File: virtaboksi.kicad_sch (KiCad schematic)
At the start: 21 parts, among them J1 Conn_01x03_Female, J2 Conn_01x02_Female, J3 Conn_01x02_Female, J4 Conn_01x02_Female, J5 Conn_01x02_Female, J6 Conn_01x02_Female, J7 Conn_01x02_Female, Q1 IRF9540N, Q2 IRF9540N, Q3 IRF9540N

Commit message: Fine-tuning of the board
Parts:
- J1: renamed from J2; footprint Connector_Phoenix_MSTB:PhoenixContact_MSTBA_2,5_2-G_1x02_P5.00mm_Horizontal -> Connector_Phoenix_MC:PhoenixContact_MCV_1,5_2-G-3.81_1x02_P3.81mm_Vertical
- J2: renamed from J1; footprint Connector_Phoenix_MSTB:PhoenixContact_MSTBA_2,5_3-G_1x03_P5.00mm_Horizontal -> Connector_Phoenix_MC:PhoenixContact_MCV_1,5_3-G-3.81_1x03_P3.81mm_Vertical
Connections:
- net BAT GOOD: now also J1.2 (Pin_2), J2.1 (Pin_1); no longer J1.1 (Pin_1), J2.3 (Pin_3)
- net HOME: now also J2.3 (Pin_3); no longer J2.1 (Pin_1)
- net at F1.2: now also J1.1 (Pin_1); no longer J1.2 (Pin_2)
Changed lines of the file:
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@@
-    (stroke (width 0) (type default) (color 0 0 0 0))
-  )
-  (wire (pts (xy 165.1 113.03) (xy 163.83 113.03))
     (stroke (width 0) (type default) (color 0 0 0 0))
   )
@@
     (stroke (width 0) (type default) (color 0 0 0 0))
   )
-  (wire (pts (xy 152.4 93.98) (xy 165.1 93.98))
+  (wire (pts (xy 152.4 99.06) (xy 165.1 99.06))
     (stroke (width 0) (type default) (color 0 0 0 0))
   )
@@
     (stroke (width 0) (type default) (color 0 0 0 0))
   )
-  (wire (pts (xy 149.86 99.06) (xy 165.1 99.06))
-    (stroke (width 0) (type default) (color 0 0 0 0))
-  )
   (wire (pts (xy 64.77 72.39) (xy 76.2 72.39))
     (stroke (width 0) (type default) (color 0 0 0 0))
@@
     (stroke (width 0) (type default) (color 0 0 0 0))
   )
+  (wire (pts (xy 165.1 110.49) (xy 163.83 110.49))
+    (stroke (width 0) (type default) (color 0 0 0 0))
+  )
   (wire (pts (xy 62.23 49.53) (xy 64.77 49.53))
     (stroke (width 0) (type default) (color 0 0 0 0))
   )
-  (wire (pts (xy 163.83 113.03) (xy 163.83 115.57))
+  (wire (pts (xy 163.83 110.49) (xy 163.83 115.57))
     (stroke (width 0) (type default) (color 0 0 0 0))
   )
@@
     (stroke (width 0) (type default) (color 0 0 0 0))
   )
+  (wire (pts (xy 165.1 93.98) (xy 149.86 93.98))
+    (stroke (width 0) (type default) (color 0 0 0 0))
+  )
   (wire (pts (xy 76.2 72.39) (xy 76.2 78.74))
     (stroke (width 0) (type default) (color 0 0 0 0))
@@
     (stroke (width 0) (type default) (color 0 0 0 0))
   )
+  (wire (pts (xy 165.1 113.03) (xy 149.86 113.03))
+    (stroke (width 0) (type default) (color 0 0 0 0))
+  )
   (wire (pts (xy 44.45 49.53) (xy 54.61 49.53))
     (stroke (width 0) (type default) (color 0 0 0 0))
   )
-  (wire (pts (xy 149.86 110.49) (xy 149.86 99.06))
+  (wire (pts (xy 149.86 93.98) (xy 149.86 113.03))
     (stroke (width 0) (type default) (color 0 0 0 0))
   )
@@
   )
   (wire (pts (xy 62.23 83.82) (xy 64.77 83.82))
-    (stroke (width 0) (type default) (color 0 0 0 0))
-  )
-  (wire (pts (xy 149.86 110.49) (xy 165.1 110.49))
     (stroke (width 0) (type default) (color 0 0 0 0))
   )
@@
     (effects (font (size 1.27 1.27)) (justify left bottom))
   )
-  (label "BAT GOOD" (at 152.4 110.49 0)
+  (label "BAT GOOD" (at 152.4 113.03 0)
     (effects (font (size 1.27 1.27)) (justify left bottom))
   )
@@
     (effects (font (size 1.27 1.27)) (justify left bottom))
   )
-  (label "HOME" (at 152.4 93.98 0)
+  (label "HOME" (at 152.4 99.06 0)
     (effects (font (size 1.27 1.27)) (justify left bottom))
   )
@@
   (symbol (lib_id "Connector:Conn_01x03_Female") (at 170.18 96.52 0) (unit 1)
     (in_bom yes) (on_board yes) (fields_autoplaced)
-    (property "Reference" "J1" (id 0) (at 170.8912 95.6853 0)
+    (property "Reference" "J2" (id 0) (at 170.8912 95.6853 0)
       (effects (font (size 1.27 1.27)) (justify left))
     )
@@
       (effects (font (size 1.27 1.27)) (justify left))
     )
-    (property "Footprint" "Connector_Phoenix_MSTB:PhoenixContact_MSTBA_2,5_3-G_1x03_P5.00mm_Horizontal" (id 2) (at 170.18 96.52 0)
+    (property "Footprint" "Connector_Phoenix_MC:PhoenixContact_MCV_1,5_3-G-3.81_1x03_P3.81mm_Vertical" (id 2) (at 170.18 96.52 0)
       (effects (font (size 1.27 1.27)) hide)
     )
@@
   (symbol (lib_id "Connector:Conn_01x02_Female") (at 170.18 110.49 0) (unit 1)
     (in_bom yes) (on_board yes)
-    (property "Reference" "J2" (id 0) (at 170.8912 110.9253 0)
+    (property "Reference" "J1" (id 0) (at 170.8912 110.9253 0)
       (effects (font (size 1.27 1.27)) (justify left))
     )
@@
       (effects (font (size 1.27 1.27)) (justify left))
     )
-    (property "Footprint" "Connector_Phoenix_MSTB:PhoenixContact_MSTBA_2,5_2-G_1x02_P5.00mm_Horizontal" (id 2) (at 170.18 110.49 0)
+    (property "Footprint" "Connector_Phoenix_MC:PhoenixContact_MCV_1,5_2-G-3.81_1x02_P3.81mm_Vertical" (id 2) (at 170.18 110.49 0)
       (effects (font (size 1.27 1.27)) hide)
     )
@@
       (reference "F1") (unit 1) (value "Fuse") (footprint "Fuse:Fuseholder_Cylinder-5x20mm_Schurter_0031_8201_Horizontal_Open")
     )
+    (path "/ebe01f49-4369-4282-9668-2fd2aa376f1c"
+      (reference "J1") (unit 1) (value "Conn_01x02_Female") (footprint "Connector_Phoenix_MC:PhoenixContact_MCV_1,5_2-G-3.81_1x02_P3.81mm_Vertical")
+    )
     (path "/59be0514-b900-4732-bd69-35f031e84c9d"
-      (reference "J1") (unit 1) (value "Conn_01x03_Female") (footprint "Connector_Phoenix_MSTB:PhoenixContact_MSTBA_2,5_3-G_1x03_P5.00mm_Horizontal")
-    )
-    (path "/ebe01f49-4369-4282-9668-2fd2aa376f1c"
-      (reference "J2") (unit 1) (value "Conn_01x02_Female") (footprint "Connector_Phoenix_MSTB:PhoenixContact_MSTBA_2,5_2-G_1x02_P5.00mm_Horizontal")
+      (reference "J2") (unit 1) (value "Conn_01x03_Female") (footprint "Connector_Phoenix_MC:PhoenixContact_MCV_1,5_3-G-3.81_1x03_P3.81mm_Vertical")
     )
     (path "/590d2007-4432-4cf1-bed4-e278a0f0bbe5"

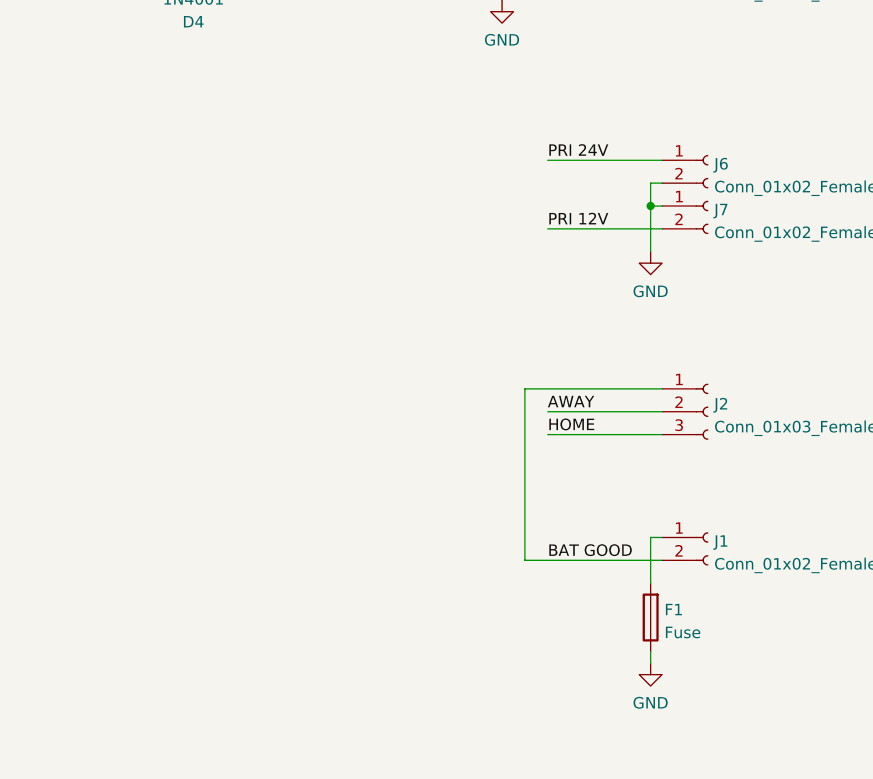
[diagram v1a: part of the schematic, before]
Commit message: Finetuning layout & adding TVS diode
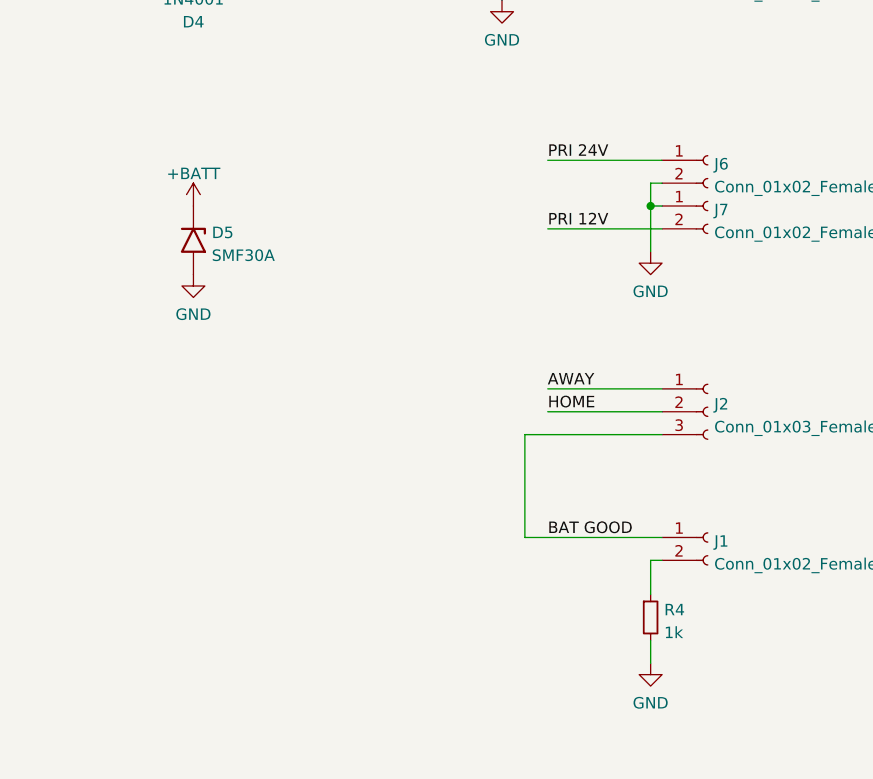
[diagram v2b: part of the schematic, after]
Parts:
- removed F1: Fuse, Fuse:Fuseholder_Cylinder-5x20mm_Schurter_0031_8201_Horizontal_Open, symbol Device:Fuse
- added D5: SMF30A, Diode_SMD:D_SMC_Handsoldering, symbol Diode:SMF30A
- added R4: 1k, Resistor_THT:R_Axial_DIN0204_L3.6mm_D1.6mm_P2.54mm_Vertical, symbol Device:R_Small
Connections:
- net +BATT: now also D5.1 (A1)
- net AWAY: now also J2.1 (Pin_1); no longer J2.2 (Pin_2)
- net BAT GOOD: now also J1.1 (Pin_1), J2.3 (Pin_3); no longer J1.2 (Pin_2), J2.1 (Pin_1)
- net GND: now also D5.2 (A2), R4.2
- net HOME: now also J2.2 (Pin_2); no longer J2.3 (Pin_3)
- new net: J1.2 (Pin_2), R4.1
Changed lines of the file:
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@@
+    (stroke (width 0) (type default) (color 0 0 0 0))
+  )
+  (wire (pts (xy 149.86 99.06) (xy 149.86 110.49))
     (stroke (width 0) (type default) (color 0 0 0 0))
   )
@@
     (stroke (width 0) (type default) (color 0 0 0 0))
   )
-  (wire (pts (xy 152.4 99.06) (xy 165.1 99.06))
+  (wire (pts (xy 149.86 99.06) (xy 165.1 99.06))
     (stroke (width 0) (type default) (color 0 0 0 0))
   )
@@
     (stroke (width 0) (type default) (color 0 0 0 0))
   )
+  (wire (pts (xy 152.4 93.98) (xy 165.1 93.98))
+    (stroke (width 0) (type default) (color 0 0 0 0))
+  )
   (wire (pts (xy 64.77 40.64) (xy 64.77 38.1))
     (stroke (width 0) (type default) (color 0 0 0 0))
@@
     (stroke (width 0) (type default) (color 0 0 0 0))
   )
+  (wire (pts (xy 165.1 113.03) (xy 163.83 113.03))
+    (stroke (width 0) (type default) (color 0 0 0 0))
+  )
   (wire (pts (xy 152.4 49.53) (xy 165.1 49.53))
     (stroke (width 0) (type default) (color 0 0 0 0))
   )
-  (wire (pts (xy 165.1 110.49) (xy 163.83 110.49))
+  (wire (pts (xy 149.86 110.49) (xy 165.1 110.49))
     (stroke (width 0) (type default) (color 0 0 0 0))
   )
@@
     (stroke (width 0) (type default) (color 0 0 0 0))
   )
-  (wire (pts (xy 163.83 110.49) (xy 163.83 115.57))
-    (stroke (width 0) (type default) (color 0 0 0 0))
-  )
   (wire (pts (xy 68.58 49.53) (xy 64.77 49.53))
     (stroke (width 0) (type default) (color 0 0 0 0))
@@
     (stroke (width 0) (type default) (color 0 0 0 0))
   )
-  (wire (pts (xy 163.83 123.19) (xy 163.83 124.46))
-    (stroke (width 0) (type default) (color 0 0 0 0))
-  )
-  (wire (pts (xy 165.1 93.98) (xy 149.86 93.98))
+  (wire (pts (xy 163.83 121.92) (xy 163.83 124.46))
     (stroke (width 0) (type default) (color 0 0 0 0))
   )
@@
     (stroke (width 0) (type default) (color 0 0 0 0))
   )
+  (wire (pts (xy 163.83 113.03) (xy 163.83 116.84))
+    (stroke (width 0) (type default) (color 0 0 0 0))
+  )
   (wire (pts (xy 76.2 92.71) (xy 76.2 88.9))
     (stroke (width 0) (type default) (color 0 0 0 0))
@@
     (stroke (width 0) (type default) (color 0 0 0 0))
   )
-  (wire (pts (xy 165.1 113.03) (xy 149.86 113.03))
-    (stroke (width 0) (type default) (color 0 0 0 0))
-  )
   (wire (pts (xy 44.45 49.53) (xy 54.61 49.53))
-    (stroke (width 0) (type default) (color 0 0 0 0))
-  )
-  (wire (pts (xy 149.86 93.98) (xy 149.86 113.03))
     (stroke (width 0) (type default) (color 0 0 0 0))
   )
@@
     (effects (font (size 1.27 1.27)) (justify left bottom))
   )
-  (label "BAT GOOD" (at 152.4 113.03 0)
+  (label "BAT GOOD" (at 152.4 110.49 0)
     (effects (font (size 1.27 1.27)) (justify left bottom))
   )
@@
     (effects (font (size 1.27 1.27)) (justify left bottom))
   )
-  (label "AWAY" (at 152.4 96.52 0)
+  (label "AWAY" (at 152.4 93.98 0)
     (effects (font (size 1.27 1.27)) (justify left bottom))
   )
@@
     (effects (font (size 1.27 1.27)) (justify left bottom))
   )
-  (label "HOME" (at 152.4 99.06 0)
+  (label "HOME" (at 152.4 96.52 0)
     (effects (font (size 1.27 1.27)) (justify left bottom))
   )
@@
     (pin "2")
   )
+  (symbol (lib_id "Diode:SMF30A") (at 113.03 77.47 270) (unit 1)
+    (in_bom yes) (on_board yes) (fields_autoplaced)
+    (property "Reference" "D5" (id 0) (at 115.062 76.6353 90)
+      (effects (font (size 1.27 1.27)) (justify left))
+    )
+    (property "Value" "SMF30A" (id 1) (at 115.062 79.1722 90)
+      (effects (font (size 1.27 1.27)) (justify left))
+    )
+    (property "Footprint" "Diode_SMD:D_SMC_Handsoldering" (id 2) (at 107.95 77.47 0)
+      (effects (font (size 1.27 1.27)) hide)
+    )
+    (property "Datasheet" "https://www.vishay.com/doc?85881" (id 3) (at 113.03 76.2 0)
+      (effects (font (size 1.27 1.27)) hide)
+    )
+    (pin "1")
+    (pin "2")
+  )
   (symbol (lib_id "Connector:Conn_01x02_Female") (at 170.18 41.91 0) (unit 1)
     (in_bom yes) (on_board yes) (fields_autoplaced)
@@
     (pin "2")
   )
-  (symbol (lib_id "Device:Fuse") (at 163.83 119.38 180) (unit 1)
-    (in_bom yes) (on_board yes) (fields_autoplaced)
-    (property "Reference" "F1" (id 0) (at 165.354 118.5453 0)
-      (effects (font (size 1.27 1.27)) (justify right))
-    )
-    (property "Value" "Fuse" (id 1) (at 165.354 121.0822 0)
-      (effects (font (size 1.27 1.27)) (justify right))
-    )
-    (property "Footprint" "Fuse:Fuseholder_Cylinder-5x20mm_Schurter_0031_8201_Horizontal_Open" (id 2) (at 165.608 119.38 90)
-      (effects (font (size 1.27 1.27)) hide)
-    )
-    (property "Datasheet" "~" (id 3) (at 163.83 119.38 0)
-      (effects (font (size 1.27 1.27)) hide)
-    )
-    (pin "1")
-    (pin "2")
+  (symbol (lib_id "power:GND") (at 113.03 81.28 0) (unit 1)
+    (in_bom yes) (on_board yes) (fields_autoplaced)
+    (property "Reference" "#PWR010" (id 0) (at 113.03 87.63 0)
+      (effects (font (size 1.27 1.27)) hide)
+    )
+    (property "Value" "GND" (id 1) (at 113.03 85.7234 0))
+    (property "Footprint" "" (id 2) (at 113.03 81.28 0)
+      (effects (font (size 1.27 1.27)) hide)
+    )
+    (property "Datasheet" "" (id 3) (at 113.03 81.28 0)
+      (effects (font (size 1.27 1.27)) hide)
+    )
+    (pin "1")
   )
   (symbol (lib_id "power:+BATT") (at 76.2 69.85 0) (unit 1)
@@
     (pin "2")
     (pin "3")
+  )
+  (symbol (lib_id "Device:R_Small") (at 163.83 119.38 0) (unit 1)
+    (in_bom yes) (on_board yes) (fields_autoplaced)
+    (property "Reference" "R4" (id 0) (at 165.3286 118.5453 0)
+      (effects (font (size 1.27 1.27)) (justify left))
+    )
+    (property "Value" "1k" (id 1) (at 165.3286 121.0822 0)
+      (effects (font (size 1.27 1.27)) (justify left))
+    )
+    (property "Footprint" "Resistor_THT:R_Axial_DIN0204_L3.6mm_D1.6mm_P2.54mm_Vertical" (id 2) (at 163.83 119.38 0)
+      (effects (font (size 1.27 1.27)) hide)
+    )
+    (property "Datasheet" "~" (id 3) (at 163.83 119.38 0)
+      (effects (font (size 1.27 1.27)) hide)
+    )
+    (pin "1")
+    (pin "2")
   )
   (symbol (lib_id "Transistor_FET:IRF9540N") (at 73.66 49.53 0) (unit 1)
@@
     (pin "1")
   )
+  (symbol (lib_id "power:+BATT") (at 113.03 73.66 0) (unit 1)
+    (in_bom yes) (on_board yes)
+    (property "Reference" "#PWR05" (id 0) (at 113.03 77.47 0)
+      (effects (font (size 1.27 1.27)) hide)
+    )
+    (property "Value" "+BATT" (id 1) (at 113.03 70.0842 0))
+    (property "Footprint" "" (id 2) (at 113.03 73.66 0)
+      (effects (font (size 1.27 1.27)) hide)
+    )
+    (property "Datasheet" "" (id 3) (at 113.03 73.66 0)
+      (effects (font (size 1.27 1.27)) hide)
+    )
+    (pin "1")
+  )
   (symbol (lib_id "power:+BATT") (at 76.2 35.56 0) (unit 1)
     (in_bom yes) (on_board yes) (fields_autoplaced)
@@
       (reference "#PWR04") (unit 1) (value "+BATT") (footprint "")
     )
+    (path "/d9a2d301-8ad5-4795-a9ce-125fa4a16dc9"
+      (reference "#PWR05") (unit 1) (value "+BATT") (footprint "")
+    )
     (path "/f55e6c00-6aec-471b-a425-8dc72945d233"
       (reference "#PWR06") (unit 1) (value "+BATT") (footprint "")
@@
       (reference "#PWR09") (unit 1) (value "GND") (footprint "")
     )
+    (path "/3a323452-4b9c-49fc-b68e-4410bb314ca2"
+      (reference "#PWR010") (unit 1) (value "GND") (footprint "")
+    )
     (path "/3cb8ac56-c6d4-427e-ab22-bd7b8acfc679"
       (reference "#PWR0101") (unit 1) (value "+BATT") (footprint "")
@@
       (reference "D4") (unit 1) (value "1N4001") (footprint "Diode_THT:D_DO-41_SOD81_P10.16mm_Horizontal")
     )
-    (path "/3a95e55d-a0dd-4f37-9a4c-f7db214b3455"
-      (reference "F1") (unit 1) (value "Fuse") (footprint "Fuse:Fuseholder_Cylinder-5x20mm_Schurter_0031_8201_Horizontal_Open")
+    (path "/2d7d0310-f97a-456e-9aaa-9289986f80f5"
+      (reference "D5") (unit 1) (value "SMF30A") (footprint "Diode_SMD:D_SMC_Handsoldering")
     )
     (path "/ebe01f49-4369-4282-9668-2fd2aa376f1c"
@@
       (reference "R3") (unit 1) (value "100k") (footprint "Resistor_THT:R_Axial_DIN0204_L3.6mm_D1.6mm_P2.54mm_Vertical")
     )
-  )
+    (path "/64f9f903-23c7-4e7e-a032-c3b8aca32034"
+      (reference "R4") (unit 1) (value "1k") (footprint "Resistor_THT:R_Axial_DIN0204_L3.6mm_D1.6mm_P2.54mm_Vertical")
+    )
+  )
